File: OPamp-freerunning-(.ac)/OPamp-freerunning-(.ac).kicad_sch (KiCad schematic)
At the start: 5 parts, among them U1 LM741

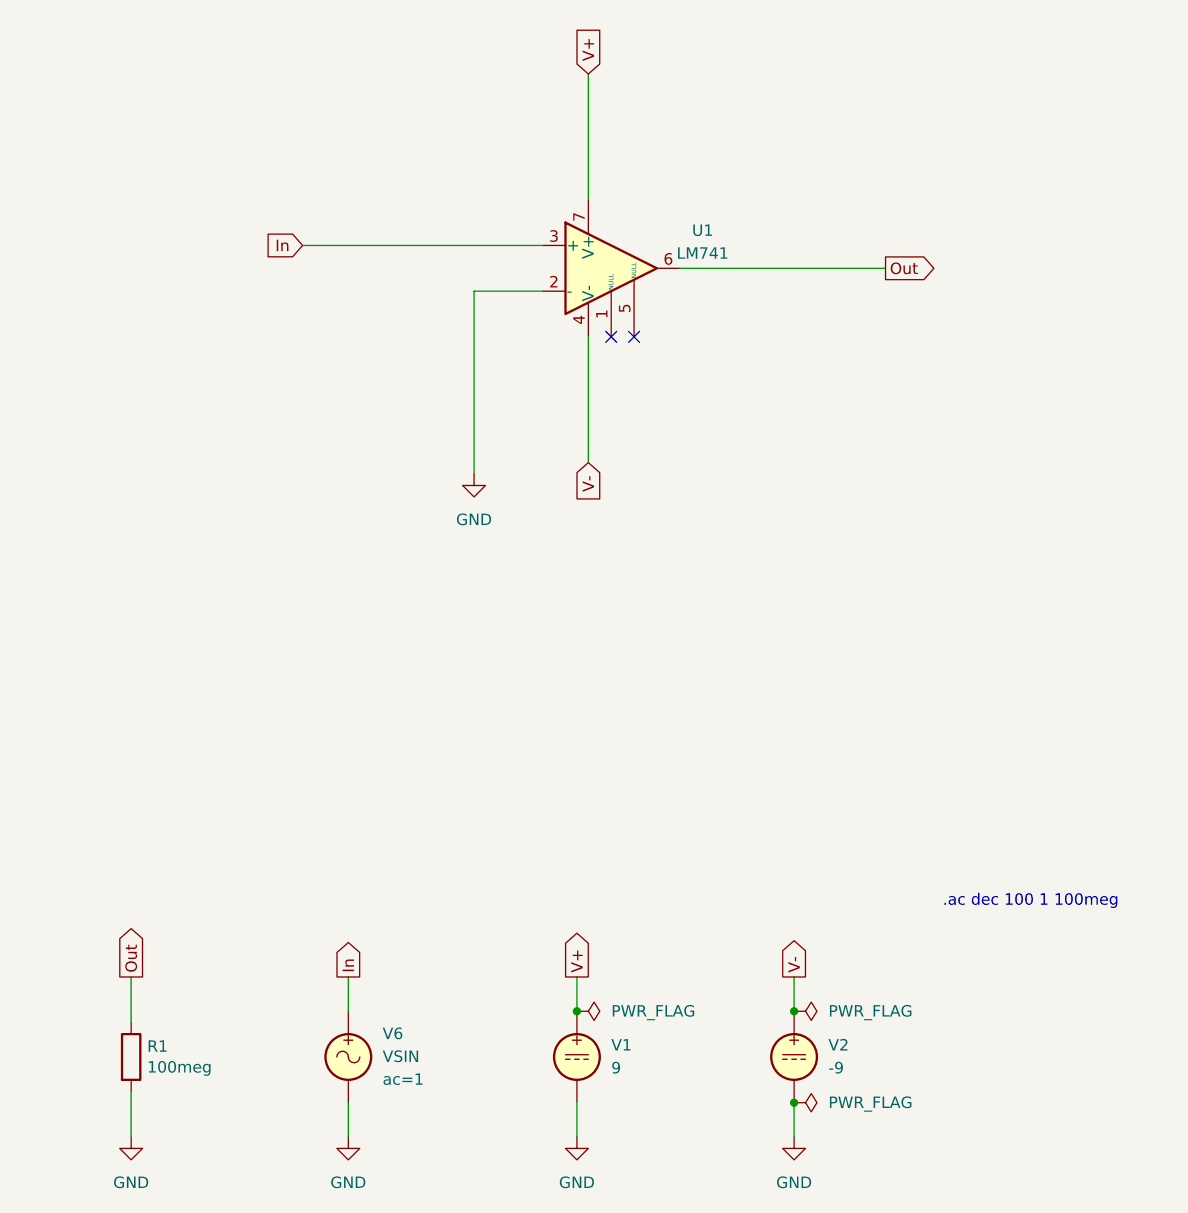
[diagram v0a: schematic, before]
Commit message: Updated all schematics and prepared for KiCad 8.0
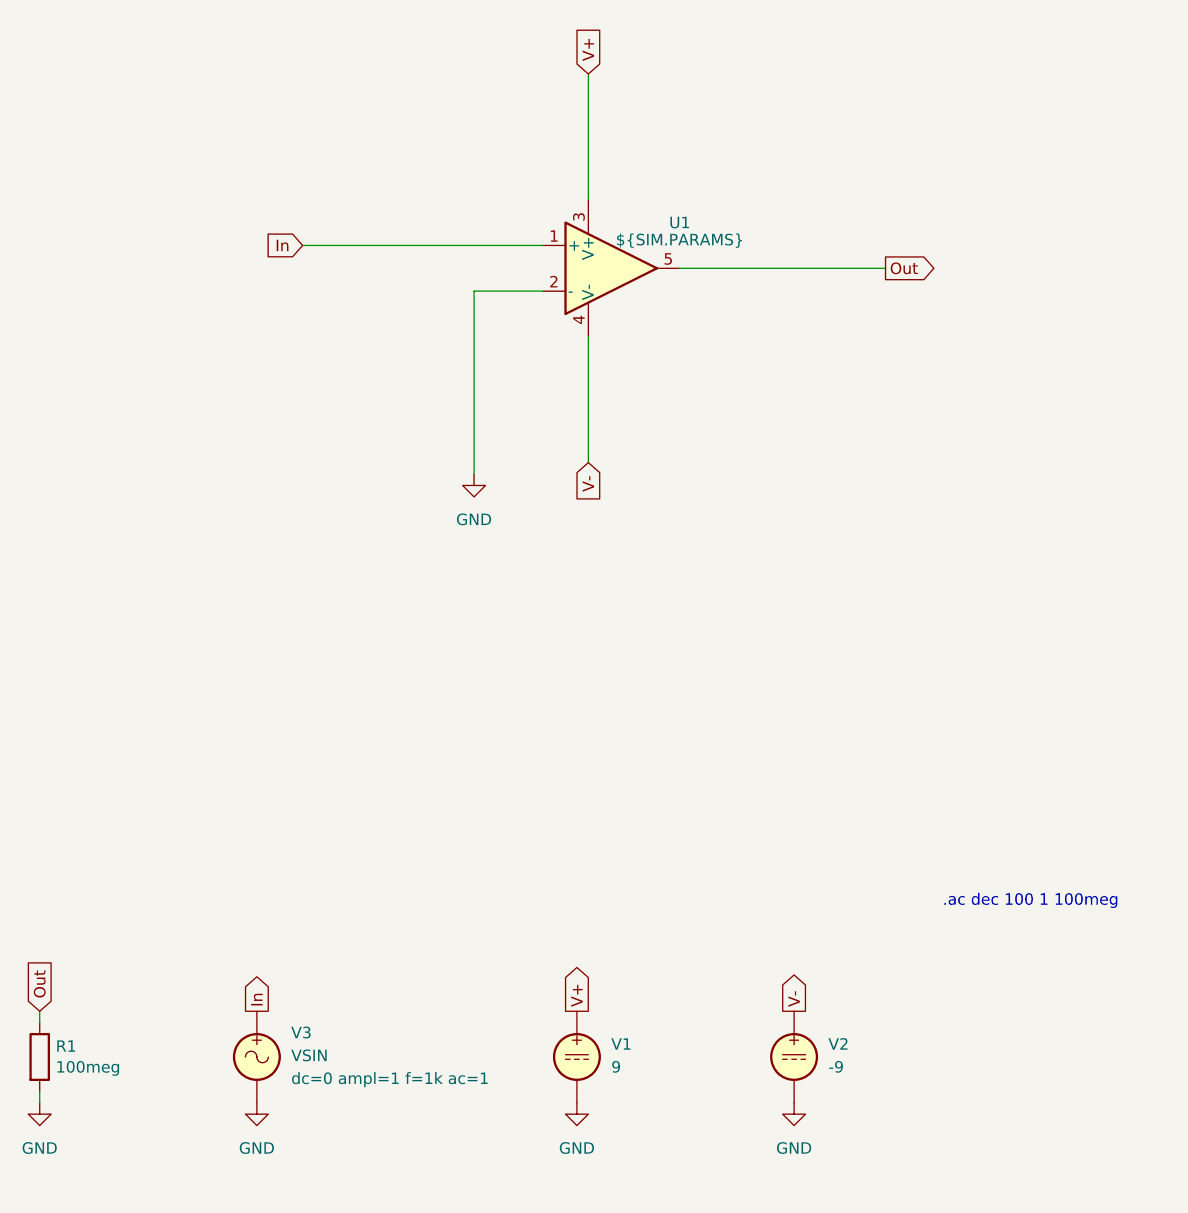
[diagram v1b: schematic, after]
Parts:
- removed U1: LM741, symbol Amplifier_Operational:LM741
- removed V6: VSIN, symbol Simulation_SPICE:VSIN
- added U1: ${SIM.PARAMS}, symbol Simulation_SPICE:OPAMP
- added V3: VSIN, symbol Simulation_SPICE:VSIN
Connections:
- net GND: now also U1.2 (-), V3.2
- net In: now also U1.1 (+), V3.1
- net Out: now also U1.5
- net V+: now also U1.3 (V+)
- net V-: now also U1.4 (V-)
- no-connect marks 2 -> 0
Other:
- moved on the sheet: R1
